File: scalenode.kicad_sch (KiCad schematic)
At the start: 2 parts

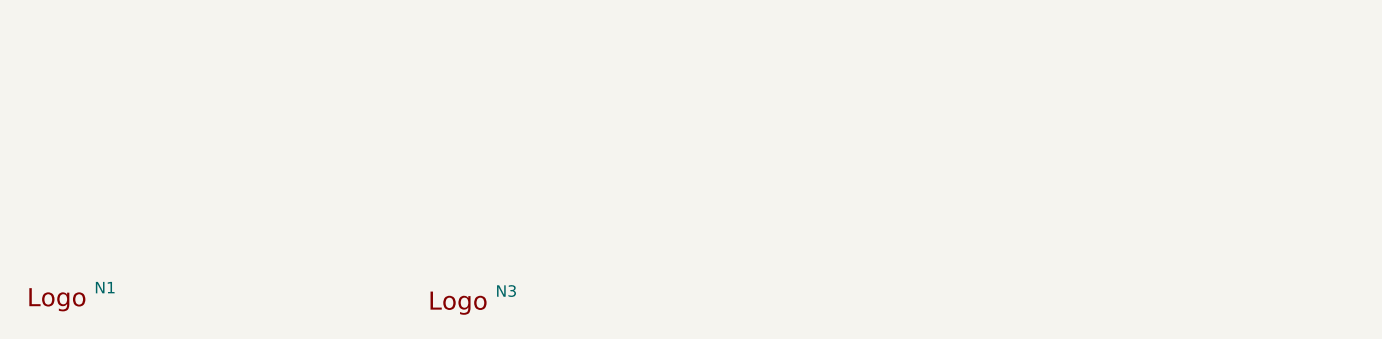
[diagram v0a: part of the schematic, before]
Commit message: Exchanged flyback to CUI DCDC converter on schematics. Added logos.
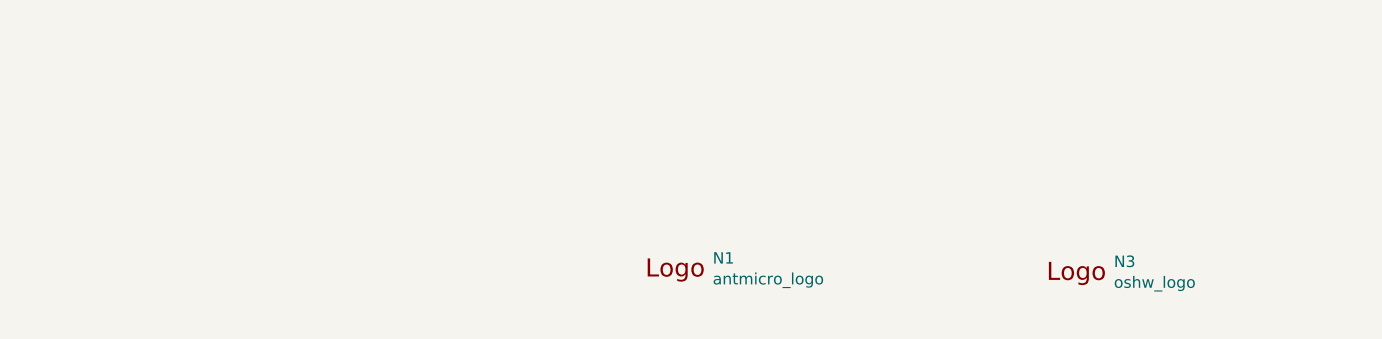
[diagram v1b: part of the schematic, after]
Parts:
- N1: value (none) -> antmicro_logo; footprint scalenode-footprints: -> scalenode-footprints:antmicro-logo_scaled_15mm
- N3: value (none) -> oshw_logo; footprint scalenode-footprints: -> scalenode-footprints:oshw-logo
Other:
- moved on the sheet: N1, N3

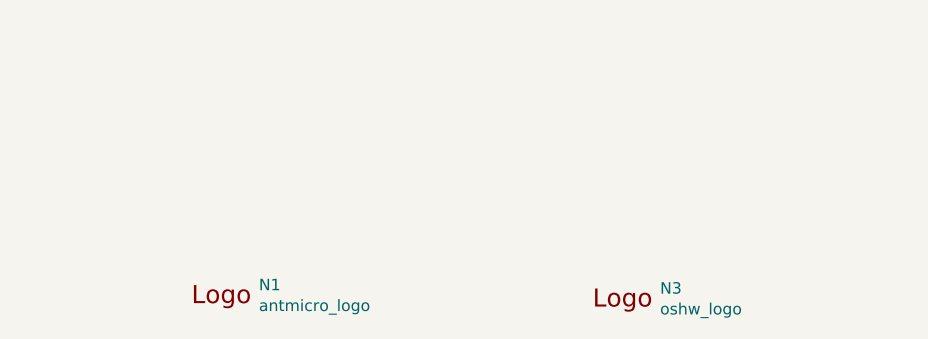
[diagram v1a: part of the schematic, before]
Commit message: Implemented changes from rev 1.0.4. New components initial placement
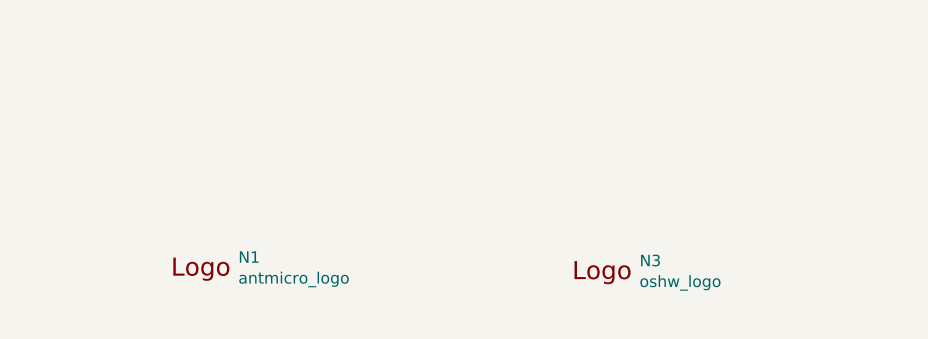
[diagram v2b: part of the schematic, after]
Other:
- moved on the sheet: N1, N3
